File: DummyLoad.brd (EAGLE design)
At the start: 39.4 x 38.1 mm, 34 parts, among them IC1 LM358, J1 BINDING-POST, J10 PINHD-1X1, J2 BINDING-POST, J3 PINHD-1X1, J4 PINHD-1X1, J5 PINHD-1X1, J6 POWERJACK-OFFBRD, J7 PINHD-1X1, J8 PINHD-1X1, J9 PINHD-1X1, Q1 NTE2390, SW1 SWITCH-SPDT-OFFBRD, SW2 SWITCH-SPDT-OFFBRD, U1 LP2950

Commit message: Design updates
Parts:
- removed J1, J2: BINDING-POST, SaintGimp:BINDING-POST-PCB-MOUNT
- removed PM1: PANEL-METER-OFFBRD, SaintGimp:1X04
- removed Q1: NTE2390, SaintGimp:TO220BV
- added R11, R12, R13, R14, R15, R16, R17, R18, R7: 1R, SaintGimp:AXIAL-7.5MM
- R5: value 0R1 -> 1R
- moved R5 62.3 mm to (5.08, -2.54), turned to 0 degrees
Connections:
- removed net N$7: J2.P$1, Q1.P2
- net +5V: no longer PM1.1
- net GATE: no longer Q1.P1
- net GND: now also R11.P$2, R12.P$2, R13.P$2, R14.P$2, R15.P$2, R16.P$2, R17.P$2, R18.P$2, R5.P$2, R7.P$2; no longer J1.P$1, PM1.2, PM1.4, R5.P$1
- net METER: no longer PM1.3
- net SENSE: now also R11.P$1, R12.P$1, R13.P$1, R14.P$1, R15.P$1, R16.P$1, R17.P$1, R18.P$1, R5.P$1, R7.P$1; no longer Q1.P3, R5.P$2
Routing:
- net SENSE: track 33.6 -> 33.0 mm
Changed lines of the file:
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@@
 <?xml version="1.0" encoding="utf-8"?>
 <!DOCTYPE eagle SYSTEM "eagle.dtd">
-<eagle version="7.4.0">
+<eagle version="7.6.0">
 <drawing>
 <settings>
@@
 <element name="R2" library="SaintGimp" package="AXIAL-7.5MM" value="1K" x="28.575" y="12.7" rot="R90"/>
 <element name="R3" library="SaintGimp" package="AXIAL-7.5MM" value="180K" x="26.035" y="12.7" rot="R90"/>
-<element name="Q1" library="SaintGimp" package="TO220BV" value="NTE2390" x="66.04" y="22.86" rot="R270"/>
-<element name="R5" library="SaintGimp" package="AXIAL-7.5MM" value="0R1" x="66.04" y="10.16" rot="R90">
-<attribute name="VALUE" value="" x="66.04" y="10.16" size="1.778" layer="27" rot="R90" display="off"/>
-</element>
 <element name="C1" library="SaintGimp" package="CAPACITOR-5MM" value="22nF" x="17.145" y="8.89" smashed="yes">
 <attribute name="NAME" x="21.209" y="8.509" size="0.8128" layer="25"/>
 <attribute name="VALUE" x="15.24" y="6.604" size="0.8128" layer="27"/>
 </element>
-<element name="J1" library="SaintGimp" package="BINDING-POST-PCB-MOUNT" value="BINDING-POST" x="52.07" y="11.43" rot="R270"/>
-<element name="J2" library="SaintGimp" package="BINDING-POST-PCB-MOUNT" value="BINDING-POST" x="52.07" y="31.75" rot="R270"/>
 <element name="C2" library="SaintGimp" package="CAPACITOR-5MM" value="0.1uF" x="17.145" y="21.59" smashed="yes">
 <attribute name="NAME" x="21.209" y="21.209" size="0.8128" layer="25"/>
@@
 <attribute name="VALUE" x="23.876" y="17.907" size="0.8128" layer="27" ratio="10" rot="R270"/>
 </element>
-<element name="PM1" library="SaintGimp" package="1X04" value="PANEL-METER-OFFBRD" x="63.5" y="39.37"/>
 <element name="J7" library="SaintGimp" package="1X01" value="PINHD-1X1" x="10.795" y="33.02" smashed="yes">
 <attribute name="VALUE" x="9.525" y="30.6491625" size="0.8128" layer="27"/>
@@
 <element name="R9" library="SaintGimp" package="AXIAL-7.5MM" value="330" x="33.655" y="12.7" rot="R270"/>
 <element name="R10" library="SaintGimp" package="AXIAL-7.5MM" value="47K" x="6.985" y="8.89"/>
+<element name="R5" library="SaintGimp" package="AXIAL-7.5MM" value="1R" x="5.08" y="-2.54"/>
+<element name="R7" library="SaintGimp" package="AXIAL-7.5MM" value="1R" x="5.08" y="-6.35"/>
+<element name="R11" library="SaintGimp" package="AXIAL-7.5MM" value="1R" x="5.08" y="-10.16"/>
+<element name="R12" library="SaintGimp" package="AXIAL-7.5MM" value="1R" x="5.08" y="-13.97"/>
+<element name="R13" library="SaintGimp" package="AXIAL-7.5MM" value="1R" x="5.08" y="-17.78"/>
+<element name="R14" library="SaintGimp" package="AXIAL-7.5MM" value="1R" x="5.08" y="-21.59"/>
+<element name="R15" library="SaintGimp" package="AXIAL-7.5MM" value="1R" x="5.08" y="-25.4"/>
+<element name="R16" library="SaintGimp" package="AXIAL-7.5MM" value="1R" x="5.08" y="-29.21"/>
+<element name="R17" library="SaintGimp" package="AXIAL-7.5MM" value="1R" x="5.08" y="-33.02"/>
+<element name="R18" library="SaintGimp" package="AXIAL-7.5MM" value="1R" x="5.08" y="-36.83"/>
 </elements>
 <signals>
@@
 <contactref element="RV1" pad="1"/>
 <contactref element="C3" pad="2"/>
-<contactref element="R5" pad="P$1"/>
-<contactref element="J1" pad="P$1"/>
-<contactref element="J5" pad="1"/>
 <contactref element="U1" pad="2"/>
 <contactref element="C4" pad="-"/>
 <contactref element="C5" pad="-"/>
-<contactref element="PM1" pad="4"/>
-<contactref element="PM1" pad="2"/>
 <contactref element="J8" pad="1"/>
 <contactref element="J9" pad="1"/>
@@
 <vertex x="1.27" y="1.27"/>
 </polygon>
-<wire x1="62.23" y1="39.37" x2="67.31" y2="39.37" width="0" layer="19" extent="1-1"/>
-<wire x1="62.23" y1="11.43" x2="62.23" y2="39.37" width="0" layer="19" extent="1-1"/>
-<wire x1="66.04" y1="6.35" x2="62.23" y2="11.43" width="0" layer="19" extent="1-1"/>
-<wire x1="33.655" y1="8.89" x2="62.23" y2="11.43" width="0" layer="19" extent="1-1"/>
+<contactref element="R5" pad="P$2"/>
+<contactref element="R17" pad="P$2"/>
+<contactref element="R13" pad="P$2"/>
+<contactref element="R18" pad="P$2"/>
+<contactref element="R12" pad="P$2"/>
+<contactref element="R14" pad="P$2"/>
+<contactref element="R15" pad="P$2"/>
+<contactref element="R16" pad="P$2"/>
+<contactref element="R11" pad="P$2"/>
+<contactref element="J5" pad="1"/>
+<contactref element="R7" pad="P$2"/>
+<wire x1="8.89" y1="-33.02" x2="8.89" y2="-36.83" width="0" layer="19" extent="1-1"/>
+<wire x1="8.89" y1="-29.21" x2="8.89" y2="-33.02" width="0" layer="19" extent="1-1"/>
+<wire x1="8.89" y1="-25.4" x2="8.89" y2="-29.21" width="0" layer="19" extent="1-1"/>
+<wire x1="8.89" y1="-21.59" x2="8.89" y2="-25.4" width="0" layer="19" extent="1-1"/>
+<wire x1="8.89" y1="-17.78" x2="8.89" y2="-21.59" width="0" layer="19" extent="1-1"/>
+<wire x1="8.89" y1="-13.97" x2="8.89" y2="-17.78" width="0" layer="19" extent="1-1"/>
+<wire x1="8.89" y1="-10.16" x2="8.89" y2="-13.97" width="0" layer="19" extent="1-1"/>
+<wire x1="8.89" y1="-6.35" x2="8.89" y2="-10.16" width="0" layer="19" extent="1-1"/>
+<wire x1="8.89" y1="-2.54" x2="8.89" y2="-6.35" width="0" layer="19" extent="1-1"/>
+<wire x1="13.335" y1="5.08" x2="8.89" y2="-2.54" width="0" layer="19" extent="1-1"/>
 </signal>
 <signal name="GATE">
-<contactref element="Q1" pad="P1"/>
 <contactref element="R1" pad="P$1"/>
 <contactref element="J3" pad="1"/>
@@
 <wire x1="5.08" y1="7.62" x2="7.62" y2="5.08" width="0.254" layer="1"/>
 <wire x1="7.62" y1="5.08" x2="8.255" y2="5.08" width="0.254" layer="1"/>
-<wire x1="8.255" y1="5.08" x2="63.5" y2="25.4" width="0" layer="19" extent="1-1"/>
 </signal>
 <signal name="N$5">
@@
 <wire x1="20.955" y1="10.16" x2="19.685" y2="8.89" width="0.254" layer="1"/>
 </signal>
-<signal name="N$7">
-<contactref element="Q1" pad="P2"/>
-<contactref element="J2" pad="P$1"/>
-<wire x1="63.5" y1="22.86" x2="62.23" y2="31.75" width="0" layer="19" extent="1-1"/>
-</signal>
 <signal name="+5V">
 <contactref element="IC1" pad="8"/>
@@
 <contactref element="U1" pad="1"/>
 <contactref element="C5" pad="+"/>
-<contactref element="PM1" pad="1"/>
 <contactref element="J7" pad="1"/>
 <contactref element="D1" pad="A"/>
@@
 <wire x1="18.415" y1="23.495" x2="24.13" y2="23.495" width="0.254" layer="1"/>
 <wire x1="24.13" y1="23.495" x2="26.035" y2="21.59" width="0.254" layer="1"/>
-<wire x1="33.655" y1="21.59" x2="59.69" y2="39.37" width="0" layer="19" extent="1-1"/>
 </signal>
 <signal name="N$11">
@@
 </signal>
 <signal name="SENSE">
-<contactref element="R2" pad="P$2"/>
-<contactref element="J4" pad="1"/>
-<contactref element="R5" pad="P$2"/>
-<contactref element="Q1" pad="P3"/>
 <contactref element="IC1" pad="5"/>
 <wire x1="22.3774" y1="18.9484" x2="22.225" y2="19.05" width="0.254" layer="1"/>
@@
 <wire x1="9.525" y1="15.24" x2="18.415" y2="15.24" width="0.254" layer="1"/>
 <wire x1="18.415" y1="15.24" x2="22.225" y2="19.05" width="0.254" layer="1"/>
-<wire x1="28.575" y1="16.51" x2="27.94" y2="16.51" width="0.254" layer="1"/>
 <wire x1="27.94" y1="16.51" x2="26.67" y2="17.78" width="0.254" layer="1"/>
 <wire x1="26.67" y1="17.78" x2="23.495" y2="17.78" width="0.254" layer="1"/>
 <wire x1="23.495" y1="17.78" x2="22.225" y2="19.05" width="0.254" layer="1"/>
 <wire x1="8.255" y1="13.97" x2="8.255" y2="7.62" width="0.254" layer="1"/>
+<contactref element="R2" pad="P$2"/>
+<contactref element="R18" pad="P$1"/>
+<contactref element="R17" pad="P$1"/>
+<contactref element="R16" pad="P$1"/>
+<contactref element="R15" pad="P$1"/>
+<contactref element="R14" pad="P$1"/>
+<contactref element="R13" pad="P$1"/>
+<contactref element="R12" pad="P$1"/>
+<contactref element="R11" pad="P$1"/>
+<contactref element="R7" pad="P$1"/>
+<contactref element="J4" pad="1"/>
+<contactref element="R5" pad="P$1"/>
+<wire x1="27.94" y1="16.51" x2="28.575" y2="16.51" width="0" layer="19" extent="1-1"/>
+<wire x1="1.27" y1="-2.54" x2="10.795" y2="5.08" width="0" layer="19" extent="1-1"/>
+<wire x1="1.27" y1="-6.35" x2="1.27" y2="-2.54" width="0" layer="19" extent="1-1"/>
+<wire x1="1.27" y1="-10.16" x2="1.27" y2="-6.35" width="0" layer="19" extent="1-1"/>
+<wire x1="1.27" y1="-13.97" x2="1.27" y2="-10.16" width="0" layer="19" extent="1-1"/>
+<wire x1="1.27" y1="-17.78" x2="1.27" y2="-13.97" width="0" layer="19" extent="1-1"/>
+<wire x1="1.27" y1="-21.59" x2="1.27" y2="-17.78" width="0" layer="19" extent="1-1"/>
+<wire x1="1.27" y1="-25.4" x2="1.27" y2="-21.59" width="0" layer="19" extent="1-1"/>
+<wire x1="1.27" y1="-29.21" x2="1.27" y2="-25.4" width="0" layer="19" extent="1-1"/>
+<wire x1="1.27" y1="-33.02" x2="1.27" y2="-29.21" width="0" layer="19" extent="1-1"/>
+<wire x1="1.27" y1="-36.83" x2="1.27" y2="-33.02" width="0" layer="19" extent="1-1"/>
 <wire x1="8.255" y1="7.62" x2="10.795" y2="5.08" width="0.254" layer="1"/>
-<wire x1="66.04" y1="13.97" x2="63.5" y2="20.32" width="0" layer="19" extent="1-1"/>
-<wire x1="28.575" y1="16.51" x2="63.5" y2="20.32" width="0" layer="19" extent="1-1"/>
 </signal>
 <signal name="N$3">
@@
 </signal>
 <signal name="METER">
-<contactref element="PM1" pad="3"/>
 <contactref element="IC1" pad="7"/>
 <contactref element="R6" pad="P$2"/>
@@
 <wire x1="10.16" y1="26.67" x2="5.715" y2="31.115" width="0.254" layer="1"/>
 <wire x1="5.715" y1="31.115" x2="5.715" y2="33.02" width="0.254" layer="1"/>
-<wire x1="17.145" y1="25.4" x2="64.77" y2="39.37" width="0" layer="19" extent="1-1"/>
 </signal>
 <signal name="N$1">

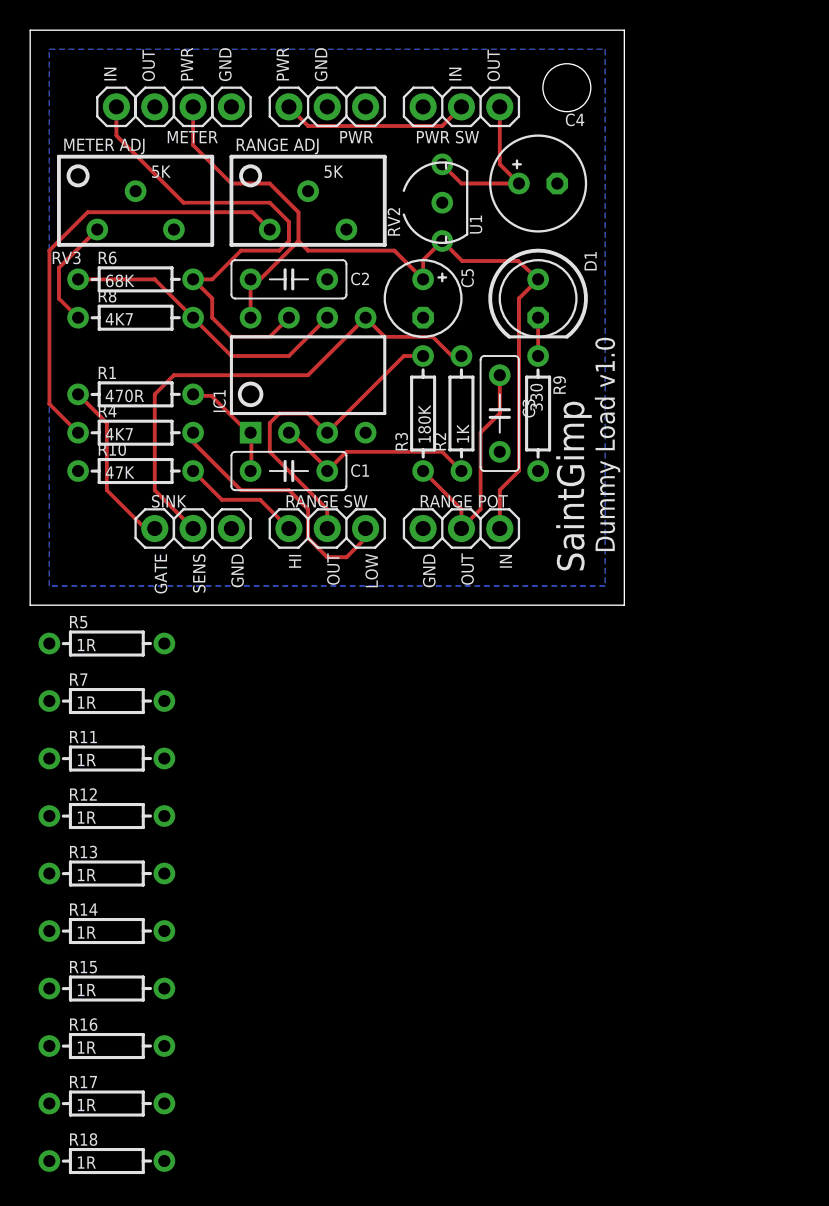
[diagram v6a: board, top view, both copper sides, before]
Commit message: Add sensor resistor array to board
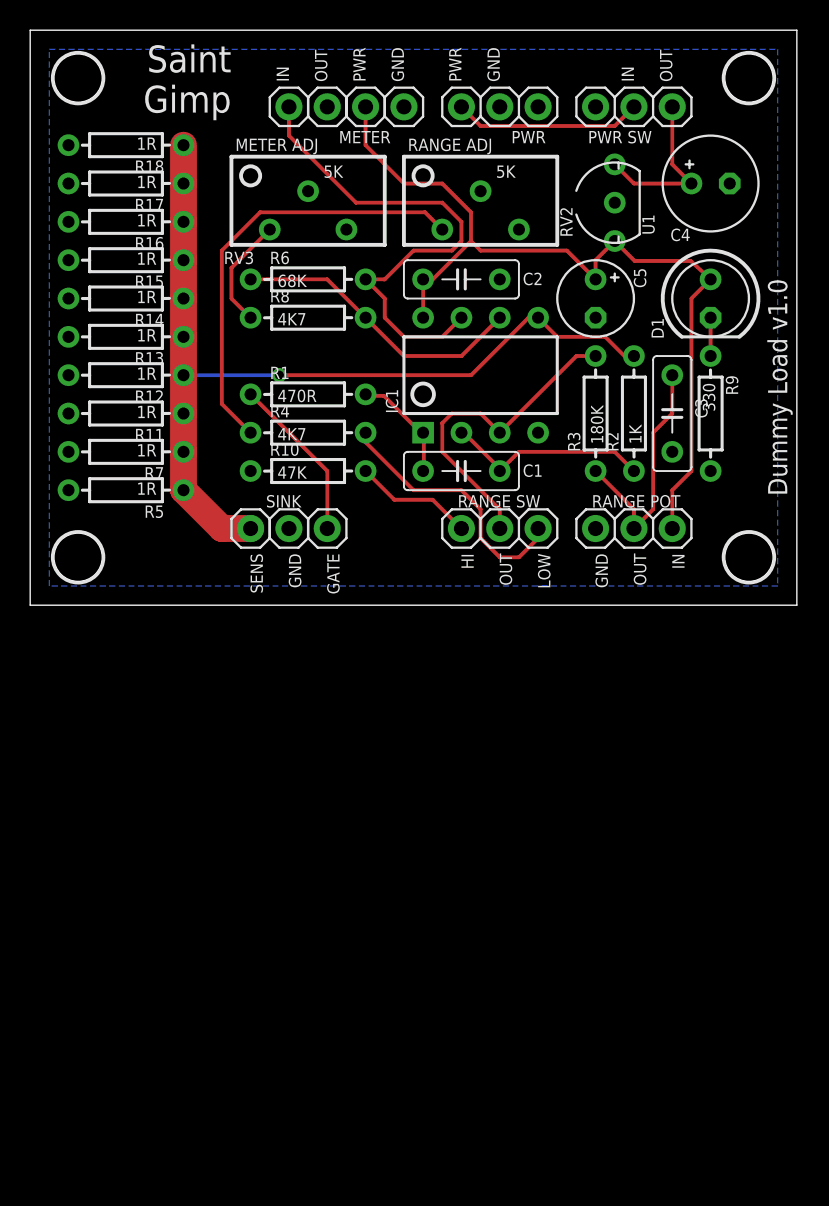
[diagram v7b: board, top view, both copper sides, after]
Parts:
- added U$1, U$2, U$3, U$4: (no value), SaintGimp:MOUNTING-HOLE-3.2MM
- moved R18 67.3 mm to (6.35, 30.5), turned to 180 degrees
- moved R17 61.0 mm to (6.35, 27.9), turned to 180 degrees
- moved R16 54.6 mm to (6.35, 25.4), turned to 180 degrees
- moved R15 48.3 mm to (6.35, 22.9), turned to 180 degrees
- moved R14 41.9 mm to (6.35, 20.3), turned to 180 degrees
- moved R13 35.6 mm to (6.35, 17.8), turned to 180 degrees
- moved R12 29.2 mm to (6.35, 15.2), turned to 180 degrees
- moved R11 22.9 mm to (6.35, 12.7), turned to 180 degrees
- moved R7 16.6 mm to (6.35, 10.2), turned to 180 degrees
- moved C3 11.4 mm to (42.5, 12.7)
- moved C5 11.4 mm to (37.5, 20.3)
- moved R2 11.4 mm to (40.0, 12.7)
- moved R3 11.4 mm to (37.5, 12.7)
- moved RV1 11.4 mm to (40.0, 5.08)
- moved SW2 11.4 mm to (40.0, 33.0)
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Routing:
- net SENSE: track 33.0 -> 60.4 mm, vias 0 -> 1
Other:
- board size 39.4 x 38.1 mm -> 50.8 x 38.1 mm
- board text added: "Saint Gimp"
- board text removed: "SaintGimp"

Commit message: Tweaked layout
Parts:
- removed J6: POWERJACK-OFFBRD, SaintGimp:1X03
- removed R10: 47K, SaintGimp:AXIAL-7.5MM
- removed SW1, SW2: SWITCH-SPDT-OFFBRD, SaintGimp:1X03
- added J1: PINHD-1X2, SaintGimp:1X02
- D1: value LED -> LED-5MM
- IC1: value LM358 -> MCP6022
- R9: value 330 -> 470
- moved R1 5.12 mm to (17.8, 8.89)
- moved J4 1.91 mm to (12.7, 5.08)
- moved RV1 1.91 mm to (38.1, 5.08)
- moved J5 1.90 mm to (15.2, 5.08)
- moved J3 1.90 mm to (17.8, 5.08)
- moved U$3 1.27 mm to (46.4, 34.9)
- moved U$4 1.27 mm to (46.4, 3.17)
- moved C3 0.64 mm to (41.9, 12.7)
- moved R2 0.64 mm to (39.4, 12.7)
- moved R3 0.64 mm to (36.8, 12.7)
- moved J7 0.64 mm to (21.6, 33.0)
- moved J8 0.64 mm to (24.1, 33.0)
- moved C1 0.63 mm to (27.9, 8.89)
- moved C2 0.63 mm to (27.9, 21.6)
- moved C4 0.63 mm to (44.5, 27.9)
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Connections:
- removed net N$1: J6.1, SW2.2
- removed net N$10: R4.P$2, SW1.3
- removed net N$9: R10.P$2, SW1.1
- net GND: now also J1.2; no longer J6.2, J6.3, R10.P$1
- net N$13: now also R4.P$2; no longer SW1.2
- net N$3: now also J1.1; no longer SW2.3
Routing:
- net N$10: track 17.5 -> 0.00 mm
- net N$1: track 12.5 -> 0.00 mm
- net N$9: track 7.93 -> 0.00 mm
- net GATE: track 11.1 -> 5.39 mm
- net N$13: track 21.7 -> 18.3 mm
- net N$3: track 11.2 -> 13.5 mm
- net SENSE: track 60.4 -> 58.5 mm
- net N$2: track 7.52 -> 6.41 mm
- net +5V: track 57.3 -> 58.4 mm
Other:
- board size 50.8 x 38.1 mm -> 49.5 x 38.1 mm
- board text added: "POT"
- board text removed: "HI"
- board text removed: "LOW"
- board text removed: "PWR SW"
- board text removed: "RANGE POT"
- board text removed: "RANGE SW"
